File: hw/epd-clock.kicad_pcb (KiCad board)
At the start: 4 copper layers, 86 x 43.7 mm, 61 parts, among them J1 Conn_01x24_MountingPin, Q1 Q_PMOS_GSD, Q2 IRLML6344, SW1 SW_Push, SW2 SW_Push, SW3 SW_Push, U1 ME2188AXXPG, U2 MSP430G2553IPW28, U3 AT25xxx, U4 PCF8563T, Y1 Crystal_Small

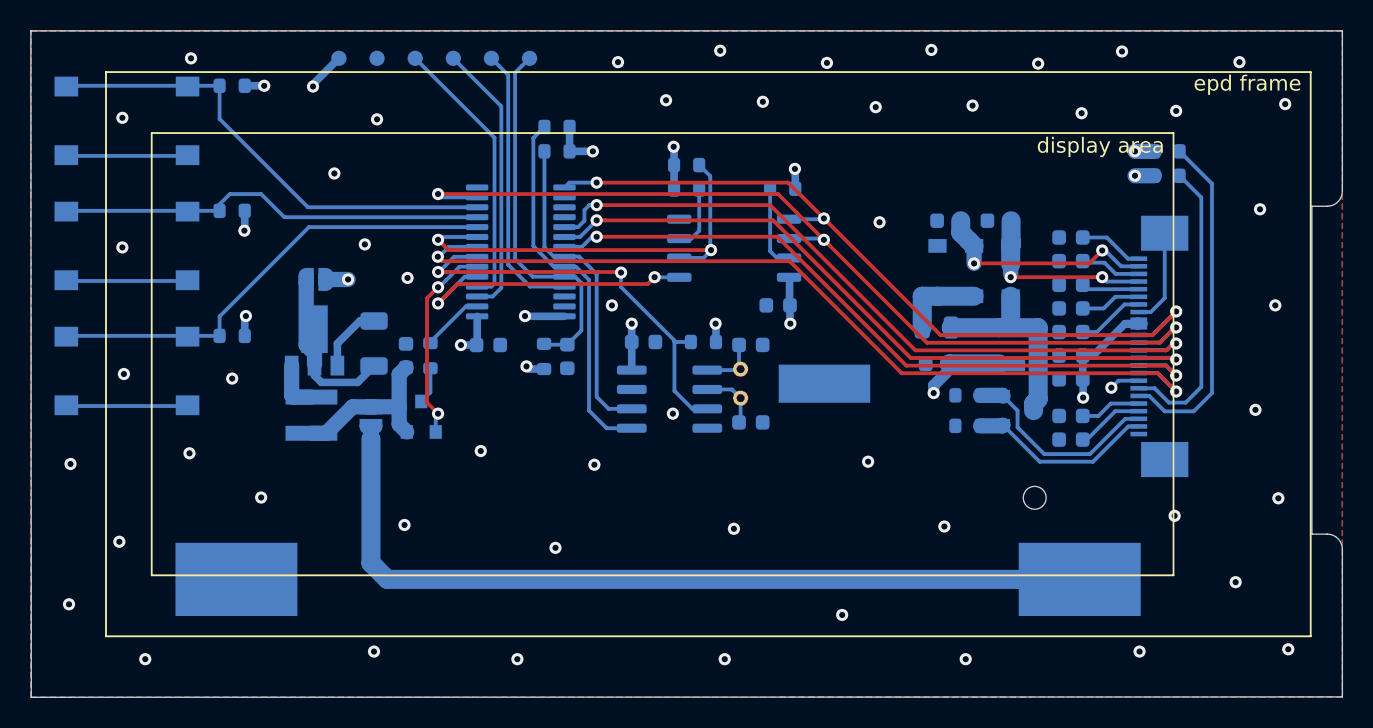
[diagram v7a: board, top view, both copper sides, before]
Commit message: Rebuild based on ESP32C3, initial work done.
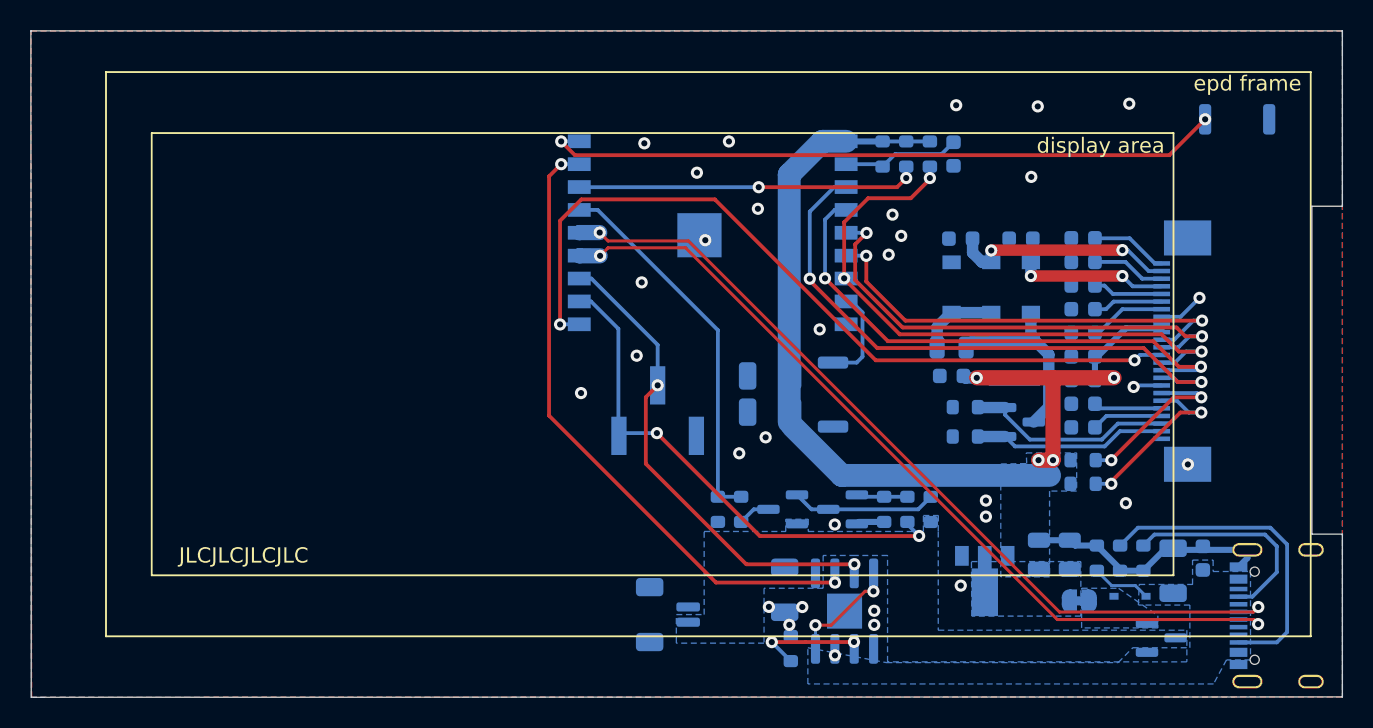
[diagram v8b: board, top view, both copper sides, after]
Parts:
- removed BT1: Battery_Cell, custom:AAA_holder_smt
- removed JP1, JP2: Jumper, Jumper:SolderJumper-2_P1.3mm_Open_RoundedPad1.0x1.5mm
- removed L2: 10uH, Inductor_SMD:L_Coilcraft_XxL4020
- removed SW3: SW_Push, Button_Switch_SMD:SW_Push_1P1T_NO_6x6mm_H9.5mm
- removed TP1, TP2, TP3, TP4, TP5, TP6: TestPoint, TestPoint:TestPoint_Pad_D1.0mm
- removed U4: PCF8563T, Package_SO:SOIC-8_3.9x4.9mm_P1.27mm
- removed Y1: Crystal_Small, Crystal:Crystal_DS26_D2.0mm_L6.0mm_Horizontal_1EP_style1
- added D4: MBR0530, Diode_SMD:D_SOD-123, B.Cu at (160.7, 114.1)
- added J2: USBC, Connector_USB:USB_C_Receptacle_Palconn_UTC16-G, B.Cu at (176.8, 135.7)
- added J3: Battery, Connector_JST:JST_SH_BM02B-SRSS-TB_1x02-1MP_P1.00mm_Vertical, B.Cu at (136.8, 135.6)
- added J4: Conn_01x24_MountingPin, Connector_FFC-FPC:TE_2-1734839-4_1x24-1MP_P0.5mm_Horizontal, B.Cu at (170.6, 118.3)
- added Q3: 3401, Package_TO_SOT_SMD:SOT-23, B.Cu at (144.4, 128.7)
- added Q4: IRLML6344, Package_TO_SOT_SMD:SOT-23, B.Cu at (159.9, 123.0)
- added R16: 4.7K, Resistor_SMD:R_0603_1608Metric, B.Cu at (164.1, 127.0)
- added R17: 0R, Jumper:SolderJumper-2_P1.3mm_Bridged_RoundedPad1.0x1.5mm, B.Cu at (163.8, 134.7)
- C1: value 10uF -> 1uF
- C10: value 4.7uF/50V -> 1uF/25V; footprint Capacitor_SMD:C_0805_2012Metric -> Capacitor_SMD:C_0603_1608Metric
- C13: value 1uF/25V -> 10uF/6V
- C15: value 1uF/6V -> 1uF/50V
- C16: value 1nF -> 1uF/25V
- C17: value 0.1uF -> 4.7uF/50V; footprint Capacitor_SMD:C_0603_1608Metric -> Capacitor_SMD:C_0805_2012Metric
- C18: value 0.1uF -> 1uF/25V
- C19: value 22pF -> 1uF/6V
- C2: value 100uF -> 0.1uF; footprint Capacitor_SMD:C_1206_3216Metric -> Capacitor_SMD:C_0603_1608Metric
- C20: value 22pF -> 100uF; footprint Capacitor_SMD:C_0603_1608Metric -> Capacitor_SMD:C_1206_3216Metric
- C21: value 0.1uF -> 10uF; footprint Capacitor_SMD:C_0603_1608Metric -> Capacitor_SMD:C_1206_3216Metric
- C3: value 0.1uF/25V -> 10uF; footprint Capacitor_SMD:C_0603_1608Metric -> Capacitor_SMD:C_1206_3216Metric
- C4: value 1uF/25V -> 10uF; footprint Capacitor_SMD:C_0603_1608Metric -> Capacitor_SMD:C_1206_3216Metric
- C5: value 1uF/25V -> 10uF; footprint Capacitor_SMD:C_0603_1608Metric -> Capacitor_SMD:C_0805_2012Metric
- C6: value 10uF/6V -> 10uF; footprint Capacitor_SMD:C_0603_1608Metric -> Capacitor_SMD:C_0805_2012Metric
- C7: value 1uF/25V -> 0.1uF/25V
- C9: value 1uF/50V -> 1uF/25V
- D1: value MBR0530 -> 1N5819; footprint Diode_SMD:D_SOD-123 -> Diode_SMD:D_SOD-323
- J1: value Conn_01x24_MountingPin -> uart; footprint Connector_FFC-FPC:TE_2-1734839-4_1x24-1MP_P0.5mm_Horizontal -> Connector_PinHeader_2.54mm:PinHeader_1x03_P2.54mm_Vertical_SMD_Pin1Left
- L1: value 22uH -> 10uH
- Q1: value Q_PMOS_GSD -> 3401
- Q2: value IRLML6344 -> 8050
- R10: value 10K -> 100K
- R11, R13: value 10K -> 4.7K
- R12: value 10K -> 1M
- R14: value 10K -> 1K
- R15: value 10K -> 3R
- R2: value 1M -> 10K
- R3: value 3R -> 10K
- R4, R5: value 4.7K -> 5.1K
- R7: value 47K -> 10K
- R8: value 4.7K -> 1K
- R9: value 4.7K -> 10K
- SW1: value SW_Push -> BT0; footprint Button_Switch_SMD:SW_Push_1P1T_NO_6x6mm_H9.5mm -> Button_Switch_SMD:SW_Push_SPST_NO_Alps_SKRK
- SW2: value SW_Push -> BT1; footprint Button_Switch_SMD:SW_Push_1P1T_NO_6x6mm_H9.5mm -> Button_Switch_SMD:SW_Push_SPST_NO_Alps_SKRK
- U1: value ME2188AXXPG -> ESP32-C3-WROOM-02; footprint Package_TO_SOT_SMD:SOT-89-3 -> custom:ESP32-C3-WROOM-02
- U2: value MSP430G2553IPW28 -> TC4056A; footprint Package_SO:TSSOP-28_4.4x9.7mm_P0.65mm -> Package_SO:HSOP-8-1EP_3.9x4.9mm_P1.27mm_EP2.3x2.3mm
- U3: value AT25xxx -> ME6210A33PG; footprint Package_SO:SOIC-8_5.275x5.275mm_P1.27mm -> Package_TO_SOT_SMD:SOT-89-3
- moved SW1 74.6 mm to (174.2, 103.1)
- moved C2 56.1 mm to (171.9, 131.9), turned to -90 degrees
- moved Q1 50.6 mm to (169.2, 137.1), turned to 0 degrees
- moved R12 48.5 mm to (156.3, 123.9), turned to 180 degrees
- moved SW2 47.3 mm to (147.7, 121.2), turned to 90 degrees
- moved L1 46.2 mm to (159.6, 118.9), turned to -90 degrees
- moved U1 42.9 mm to (153.6, 102.0), turned to 180 degrees
- moved R14 42.3 mm to (140.1, 128.7), turned to -90 degrees
- moved R13 38.7 mm to (141.7, 128.7), turned to 90 degrees
- moved R7 38.6 mm to (165.0, 131.9), turned to -90 degrees
- moved C1 38.3 mm to (155.6, 105.4)
- moved C16 34.1 mm to (164.1, 114.0), turned to 180 degrees
- moved R8 34.0 mm to (152.6, 128.7), turned to 90 degrees
- moved R9 33.9 mm to (154.1, 128.7), turned to 90 degrees
- moved J1 33.2 mm to (136.2, 122.2), turned to 90 degrees
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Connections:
- C1 pad 1: Net-(C1-Pad1) -> -BATT
- C1 pad 2: GND -> /CHIP_PU
- C10 pad 1: Net-(C10-Pad1) -> +3V3
- C10 pad 2: Net-(C10-Pad2) -> -BATT
- C11 pad 1: /epd/VPP -> /VDD
- C11 pad 2: GND -> -BATT
- C12 pad 1: /epd/PREVGL -> /PREVGH
- C12 pad 2: GND -> -BATT
- C13 pad 1: /epd/VSH -> -BATT
- C13 pad 2: GND -> +3V3
- C14 pad 1: /epd/VSL -> /VPP
- C14 pad 2: GND -> -BATT
- C15 pad 1: /epd/VCOM -> /PREVGL
- C15 pad 2: GND -> -BATT
- C16 pad 1: /mcu/RST -> /VSH
- C16 pad 2: GND -> -BATT
- C17 pad 1: +3V3 -> Net-(C17-Pad1)
- C17 pad 2: GND -> Net-(C17-Pad2)
- C18 pad 1: +3V3 -> /VSL
- C18 pad 2: GND -> -BATT
- C19 pad 1: Net-(C19-Pad1) -> /VCOM
- C19 pad 2: GND -> -BATT
- C2 pad 1: Net-(C2-Pad1) -> -BATT
- C2 pad 2: GND -> VBUS
- C20 pad 1: Net-(C20-Pad1) -> +3V3
- C20 pad 2: GND -> -BATT
- C21 pad 1: GND -> +3V3
- C21 pad 2: +3V3 -> -BATT
- C3 pad 1: +3V3 -> -BATT
- C3 pad 2: GND -> VBUS
- C4 pad 1: /epd/VGH -> -BATT
- C4 pad 2: GND -> +BATT
- C5 pad 1: /epd/VGL -> -BATT
- C5 pad 2: GND -> VCC
- C6 pad 1: GND -> -BATT
- C7 pad 2: GND -> -BATT
- C8 pad 1: /epd/VDD -> /VGH
- C8 pad 2: GND -> -BATT
- C9 pad 1: /epd/PREVGH -> /VGL
- C9 pad 2: GND -> -BATT
- D1 pad 1: GND -> Net-(D1-Pad1)
- D1 pad 2: Net-(C10-Pad2) -> VBUS
- D2 pad 1: Net-(C10-Pad2) -> -BATT
- D2 pad 2: /epd/PREVGL -> Net-(C17-Pad2)
- D3 pad 1: /epd/PREVGH -> Net-(C17-Pad2)
- D3 pad 2: Net-(C10-Pad1) -> /PREVGL
- J1 pad 1: /epd/VCOM -> -BATT
- J1 pad 2: /epd/PREVGL -> /CHRG
- J1 pad 3: /epd/VSL -> /IO20
- L1 pad 1: Net-(C1-Pad1) -> Net-(C17-Pad1)
- L1 pad 2: Net-(L1-Pad2) -> +3V3
- Q1 pad 1: /power/ADEN# -> VBUS
- Q1 pad 2: Net-(C1-Pad1) -> Net-(D1-Pad1)
- Q1 pad 3: Net-(Q1-Pad3) -> +BATT
- Q2 pad 1: /epd/GDR -> Net-(Q2-Pad1)
- Q2 pad 2: /epd/RESE -> -BATT
- Q2 pad 3: Net-(C10-Pad1) -> Net-(Q2-Pad3)
- R1 pad 1: /mcu/AIN -> +3V3
- R1 pad 2: Net-(Q1-Pad3) -> /CHIP_PU
- R10 pad 1: Net-(R10-Pad1) -> Net-(Q2-Pad1)
- R10 pad 2: +3V3 -> -BATT
- R11 pad 1: Net-(R11-Pad1) -> +3V3
- R11 pad 2: +3V3 -> /TSDA
- R12 pad 1: /button/BT0 -> /GDR
- R12 pad 2: +3V3 -> -BATT
- R13 pad 1: /button/BT1 -> Net-(Q3-Pad3)
- R13 pad 2: +3V3 -> /ADC1_CH3
- R14 pad 1: /button/BT2 -> /ADC1_CH3
- R14 pad 2: +3V3 -> -BATT
- R15 pad 1: +3V3 -> /RESE
- R15 pad 2: /rtc/INT -> -BATT
- R2 pad 1: /epd/GDR -> +3V3
- R2 pad 2: GND -> /EPD_DC
- R3 pad 1: /epd/RESE -> /FSPIQ
- R3 pad 2: GND -> +3V3
- R4 pad 1: +3V3 -> Net-(J2-PadA5)
- R4 pad 2: /epd/TSDA -> -BATT
- R5 pad 1: +3V3 -> Net-(J2-PadB5)
- R5 pad 2: /epd/TSCL -> -BATT
- R6 pad 1: +3V3 -> -BATT
- R6 pad 2: /flash/MISO -> Net-(R6-Pad2)
- R7 pad 1: +3V3 -> -BATT
- R7 pad 2: /mcu/RST -> VBUS
- R8 pad 1: +3V3 -> /IO20
- R8 pad 2: /mcu/SDA -> Net-(Q2-Pad1)
- R9 pad 1: +3V3 -> +BATT
- R9 pad 2: /mcu/SCL -> Net-(Q2-Pad3)
- SW1 pad 1: /button/BT0 -> -BATT
- SW1 pad 2: GND -> /IO0
- SW2 pad 1: /button/BT1 -> -BATT
- SW2 pad 2: GND -> /IO9
- U1 pad 1: GND -> +3V3
- U1 pad 2: Net-(C2-Pad1) -> /CHIP_PU
- U1 pad 3: Net-(L1-Pad2) -> /EPD_BUSY
- U2 pad 1: +3V3 -> -BATT
- U2 pad 2: /mcu/AIN -> Net-(R6-Pad2)
- U2 pad 3: /mcu/UCA0RXD -> -BATT
- U2 pad 4: /mcu/UCA0TXD -> VBUS
- U2 pad 5: /flash/CS -> +BATT
- U2 pad 6: /power/ADEN# -> /IO1
- U2 pad 7: /rtc/INT -> /CHRG
- U2 pad 8: /epd/BUSY -> VBUS
- U2 pad 9: /flash/MISO -> (no net)
- U3 pad 1: /flash/CS -> -BATT
- U3 pad 2: /flash/MISO -> VCC
- U3 pad 3: Net-(R10-Pad1) -> +3V3
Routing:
- net /epd/CLK: track 61.3 -> 0.00 mm, vias 3 -> 0
- net /epd/BUSY: track 57.9 -> 0.00 mm, vias 2 -> 0
- net /USB_D+: track 0.00 -> 56.5 mm, vias 0 -> 2
- net /USB_D-: track 0.00 -> 56.4 mm, vias 0 -> 2
- net Net-(BT1-Pad1): track 55.9 -> 0.00 mm
- net /EPD_CS: track 0.00 -> 52.6 mm, vias 0 -> 2
- net /epd/DIN: track 50.4 -> 0.00 mm, vias 3 -> 0
- net /epd/CS#: track 47.9 -> 0.00 mm, vias 2 -> 0
- net /mcu/EPD_RST#: track 46.9 -> 0.00 mm, vias 2 -> 0
- net /epd/DC#: track 46.8 -> 0.00 mm, vias 2 -> 0
- net /IO0: track 0.00 -> 44.8 mm, vias 0 -> 2
- net /IO1: track 0.00 -> 41.9 mm, vias 0 -> 2
- net /EPD_DC: track 0.00 -> 40.0 mm, vias 0 -> 3
- net GND: track 39.3 -> 0.00 mm, vias 54 -> 0
- net /EPD_BUSY: track 0.00 -> 38.7 mm, vias 0 -> 2
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- added copper zone on B.Cu, net +3V3
- added copper zone on B.Cu, net +BATT
- added copper zone on B.Cu, net -BATT
- added copper zone on F.Cu, net -BATT
- added copper zone on B.Cu, net Net-(D1-Pad1)
- added copper zone on B.Cu, net VBUS
- added copper zone on B.Cu, net VCC
- removed copper zone on In1.Cu.PWR, net +3V3
- removed copper zone on B.Cu, net GND
- removed copper zone on F.Cu, net GND
- removed copper zone on In2.Cu.GND, net GND
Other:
- outline, holes or cut-outs redrawn
- copper layers 4 -> 2
- net class Default removed
- net class Power removed
- board text added: "+"
- board text added: "-"
- board text added: "JLCJLCJLCJLC"
- board text added: "V0.3"
- board text removed: "3V3"
- board text removed: "Battery-TP"
- board text removed: "GND"
- board text removed: "RST"
- board text removed: "RXD"
- board text removed: "TEST"
- board text removed: "TXD"
